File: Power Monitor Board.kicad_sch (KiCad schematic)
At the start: 13 parts, among them U1 ACS709xLFTR-10BB, U10 ACS709xLFTR-10BB, U11 ACS709xLFTR-10BB, U12 ACS709xLFTR-10BB, U2 ACS709xLFTR-10BB, U3 ACS709xLFTR-10BB, U4 ACS709xLFTR-10BB, U5 ACS709xLFTR-10BB, U6 ACS709xLFTR-10BB, U7 ACS709xLFTR-10BB, U8 ACS709xLFTR-10BB, U9 ACS709xLFTR-10BB

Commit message: Add files via upload
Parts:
- removed U1, U10, U11, U12, U2, U3, U4, U5, U6, U7, U8, U9: ACS709xLFTR-10BB, Sensor_Current:Allegro_QSOP-24_3.9x8.7mm_P0.635mm, symbol Sensor_Current:ACS709xLFTR-10BB
- added J1: Conn_01x02_Socket, Connector:Banana_Jack_2Pin, symbol Connector:Conn_01x02_Socket
- added J10, J11, J2, J5, J6, J7, J8, J9: Conn_01x02_Pin, Connector_AMASS:AMASS_XT60-M_1x02_P7.20mm_Vertical, symbol Connector:Conn_01x02_Pin
- added J3, J4: Conn_01x01_Socket, Connector_PinSocket_2.54mm:PinSocket_1x01_P2.54mm_Vertical, symbol Connector:Conn_01x01_Socket
- added U1, U2, U3, U4, U5, U6, U7, U8: ACS711xLCTR-25AB, Package_SO:SOIC-8_3.9x4.9mm_P1.27mm, symbol Sensor_Current:ACS711xLCTR-25AB
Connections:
- net GND: now also J1.2 (Pin_2), J10.2 (Pin_2), J11.2 (Pin_2), J2.2 (Pin_2), J4.1 (Pin_1), J5.2 (Pin_2), J6.2 (Pin_2), J7.2 (Pin_2), J8.2 (Pin_2), J9.2 (Pin_2), U1.5 (GND), U2.5 (GND), U3.5 (GND), U4.5 (GND), U5.5 (GND), U6.5 (GND), U7.5 (GND), U8.5 (GND)
- net Arduino Mega A5: now reaches A2.A5
- net Arduino Mega A5: now also U6.7 (VIOUT)
- net Arduino Mega A1: now reaches A2.A1
- net Arduino Mega A1: now also U2.7 (VIOUT)
- net Arduino Mega A2: now reaches A2.A2
- net Arduino Mega A2: now also U3.7 (VIOUT)
- net Arduino Mega A4: now reaches A2.A4
- net Arduino Mega A4: now also U5.7 (VIOUT)
- net Arduino Mega A7: now reaches A2.A7
- net Arduino Mega A7: now also U8.7 (VIOUT)
- net Arduino Mega A6: now reaches A2.A6
- net Arduino Mega A6: now also U7.7 (VIOUT)
- net Arduino Mega A0: now reaches A2.A0
- net Arduino Mega A0: now also U1.7 (VIOUT)
- net Arduino Mega A3: now reaches A2.A3
- net Arduino Mega A3: now also U4.7 (VIOUT)
- net +5V renamed 5V VCC
- net 5V VCC: now also J3.1 (Pin_1), U1.8 (VCC), U2.8 (VCC), U3.8 (VCC), U4.8 (VCC), U5.8 (VCC), U6.8 (VCC), U7.8 (VCC), U8.8 (VCC)
- new net Motor 1 +: J2.1 (Pin_1), U1.3 (IP-), U1.4 (IP-)
- new net Motor 2 +: J5.1 (Pin_1), U2.3 (IP-), U2.4 (IP-)
- new net Motor 3 +: J6.1 (Pin_1), U3.3 (IP-), U3.4 (IP-)
- new net Motor 4 +: J7.1 (Pin_1), U4.3 (IP-), U4.4 (IP-)
- new net Motor 5 +: J8.1 (Pin_1), U5.3 (IP-), U5.4 (IP-)
- new net Motor 6 +: J9.1 (Pin_1), U6.3 (IP-), U6.4 (IP-)
- new net Motor 7 +: J10.1 (Pin_1), U7.3 (IP-), U7.4 (IP-)
- new net Motor 8 +: J11.1 (Pin_1), U8.3 (IP-), U8.4 (IP-)
- new net Power Supply +: J1.1 (Pin_1), U1.1 (IP+), U1.2 (IP+), U2.1 (IP+), U2.2 (IP+), U3.1 (IP+), U3.2 (IP+), U4.1 (IP+), U4.2 (IP+), U5.1 (IP+), U5.2 (IP+), U6.1 (IP+), U6.2 (IP+), U7.1 (IP+), U7.2 (IP+), U8.1 (IP+), U8.2 (IP+)
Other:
- moved on the sheet: A2

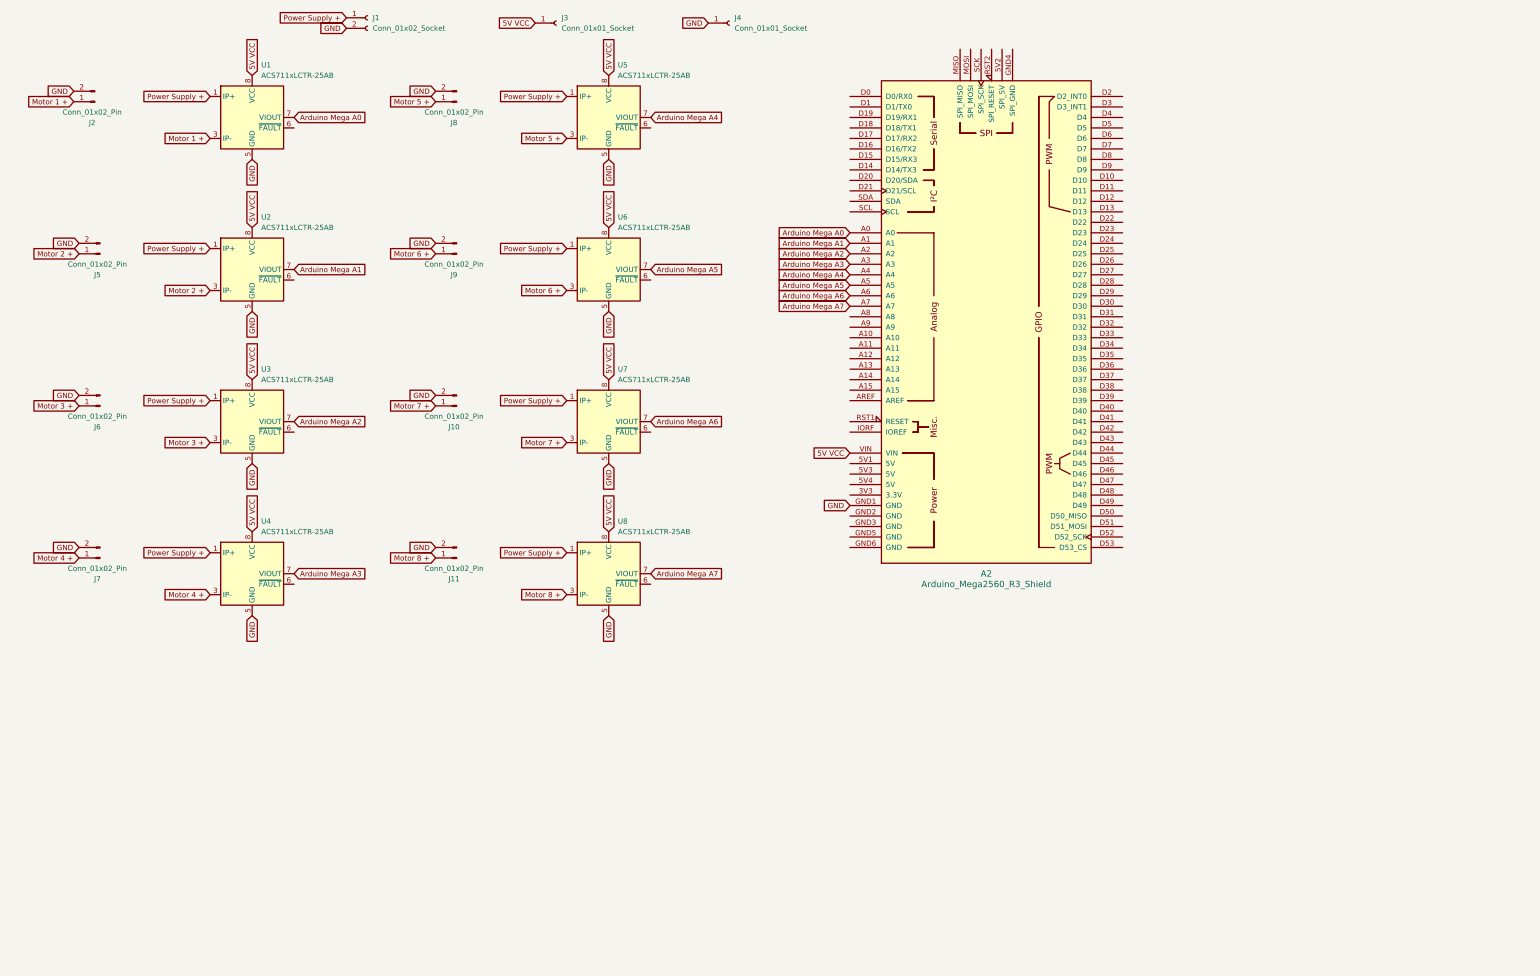
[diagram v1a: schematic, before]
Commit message: Cleaned up schematic and started layout
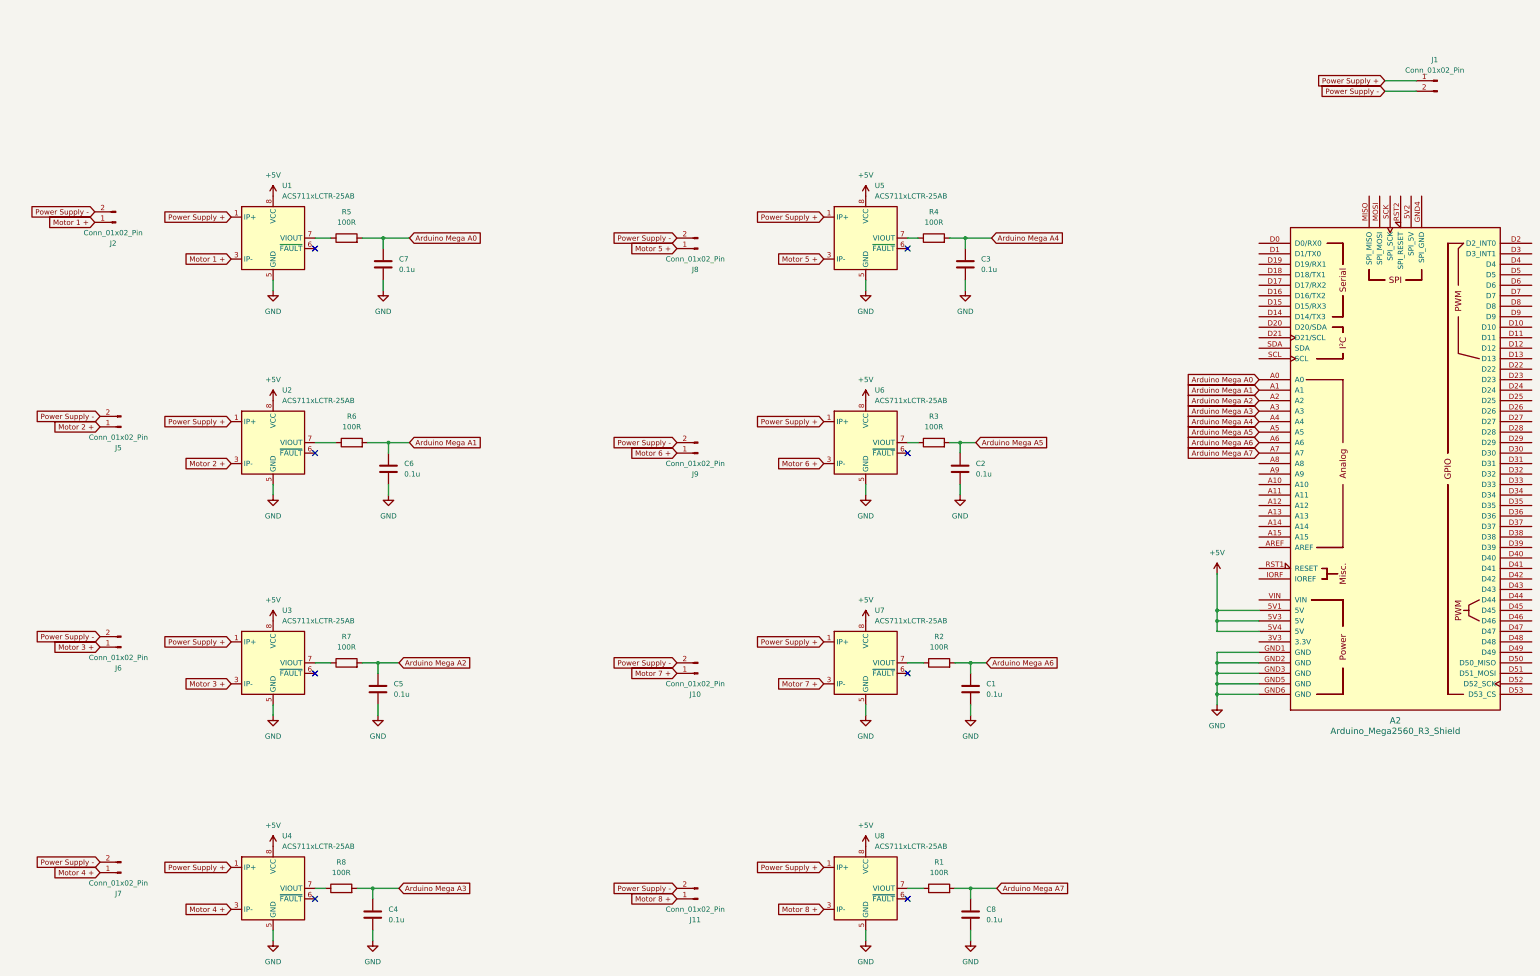
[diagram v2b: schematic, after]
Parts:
- removed J1: Conn_01x02_Socket, Connector:Banana_Jack_2Pin, symbol Connector:Conn_01x02_Socket
- removed J3, J4: Conn_01x01_Socket, Connector_PinSocket_2.54mm:PinSocket_1x01_P2.54mm_Vertical, symbol Connector:Conn_01x01_Socket
- added C1, C2, C3, C4, C5, C6, C7, C8: 0.1u, Capacitor_SMD:C_0603_1608Metric, symbol Device:C
- added J1: Conn_01x02_Pin, Connector_AMASS:AMASS_XT60-M_1x02_P7.20mm_Vertical, symbol Connector:Conn_01x02_Pin
- added R1, R2, R3, R4, R5, R6, R7, R8: 100R, Resistor_SMD:R_0603_1608Metric, symbol Device:R
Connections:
- net Arduino Mega A0: now also C7.1, R5.2; no longer U1.7 (VIOUT)
- net Arduino Mega A1: now also C6.1, R6.2; no longer U2.7 (VIOUT)
- net Arduino Mega A2: now also C5.1, R7.2; no longer U3.7 (VIOUT)
- net Arduino Mega A3: now also C4.1, R8.2; no longer U4.7 (VIOUT)
- net Arduino Mega A4: now also C3.1, R4.2; no longer U5.7 (VIOUT)
- net Arduino Mega A5: now also C2.1, R3.2; no longer U6.7 (VIOUT)
- net Arduino Mega A6: now also C1.1, R2.2; no longer U7.7 (VIOUT)
- net Arduino Mega A7: now also C8.1, R1.2; no longer U8.7 (VIOUT)
- net GND: now also A2.GND2 (GND), A2.GND3 (GND), A2.GND5 (GND), A2.GND6 (GND), C1.2, C2.2, C3.2, C4.2, C5.2, C6.2, C7.2, C8.2; no longer J10.2 (Pin_2), J11.2 (Pin_2), J2.2 (Pin_2), J5.2 (Pin_2), J6.2 (Pin_2), J7.2 (Pin_2), J8.2 (Pin_2), J9.2 (Pin_2)
- net Power Supply +: now also J1.1 (Pin_1)
- net +5V: now reaches A2.5V1 (5V)
- net +5V: now also A2.5V3 (5V), A2.5V4 (5V), U1.8 (VCC), U2.8 (VCC), U3.8 (VCC), U4.8 (VCC), U5.8 (VCC), U6.8 (VCC), U7.8 (VCC), U8.8 (VCC)
- removed net 5V VCC: A2.VIN, U1.8 (VCC), U2.8 (VCC), U3.8 (VCC), U4.8 (VCC), U5.8 (VCC), U6.8 (VCC), U7.8 (VCC), U8.8 (VCC)
- new net: R3.1, U6.7 (VIOUT)
- new net: R8.1, U4.7 (VIOUT)
- new net: R7.1, U3.7 (VIOUT)
- new net: R2.1, U7.7 (VIOUT)
- new net: R5.1, U1.7 (VIOUT)
- new net: R6.1, U2.7 (VIOUT)
- new net: R1.1, U8.7 (VIOUT)
- new net: R4.1, U5.7 (VIOUT)
- new net Power Supply -: J1.2 (Pin_2), J10.2 (Pin_2), J11.2 (Pin_2), J2.2 (Pin_2), J5.2 (Pin_2), J6.2 (Pin_2), J7.2 (Pin_2), J8.2 (Pin_2), J9.2 (Pin_2)
- no-connect marks 0 -> 8
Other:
- moved on the sheet: A2, J10, J11, J2, J5, J6, J7, J8, J9, U1, U2, U3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

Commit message: Add files via upload
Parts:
- added C10, C11, C12, C13, C14, C15, C16, C9: 0.1u, Capacitor_SMD:C_0603_1608Metric, symbol Device:C
- added NT1: NetTie_2, NetTie:NetTie-2_SMD_Pad0.5mm, symbol Device:NetTie_2
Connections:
- net +5V: now also C10.1, C11.1, C12.1, C13.1, C14.1, C15.1, C16.1, C9.1
- net GND: now also C10.2, C11.2, C12.2, C13.2, C14.2, C15.2, C16.2, C9.2, NT1.2
- net Power Supply -: now also NT1.1
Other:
- moved on the sheet: C2, C3, C7, J2, J8, J9, R3, R4, R5, U1, U5, U6

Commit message: Add files via upload
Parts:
- added C17: 0.1u, Capacitor_SMD:C_0603_1608Metric, symbol Device:C
- added R10, R9: R, Resistor_THT:R_Axial_DIN0309_L9.0mm_D3.2mm_P12.70mm_Horizontal, symbol Device:R
- added R11: 100R, Resistor_SMD:R_0603_1608Metric, symbol Device:R
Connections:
- net GND: now also C17.2, R10.2
- net Power Supply +: now also R9.1
- net Arduino Mega A8: now reaches A2.A8
- net Arduino Mega A8: now also C17.1, R11.2
- new net: R10.1, R11.1, R9.2
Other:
- moved on the sheet: A2, C1, C10, C12, C14, C16, C2, C3, C8, J1, J10, J11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
